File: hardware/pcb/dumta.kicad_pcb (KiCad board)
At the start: 2 copper layers, 111.3 x 90 mm, 48 parts, among them J2 nice_view, SW1 SW_PUSH, SW10 SW_PUSH, SW11 SW_PUSH, SW12 SW_PUSH, SW13 SW_PUSH, SW14 SW_PUSH, SW15 SW_PUSH, SW16 SW_PUSH, SW17 SW_PUSH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

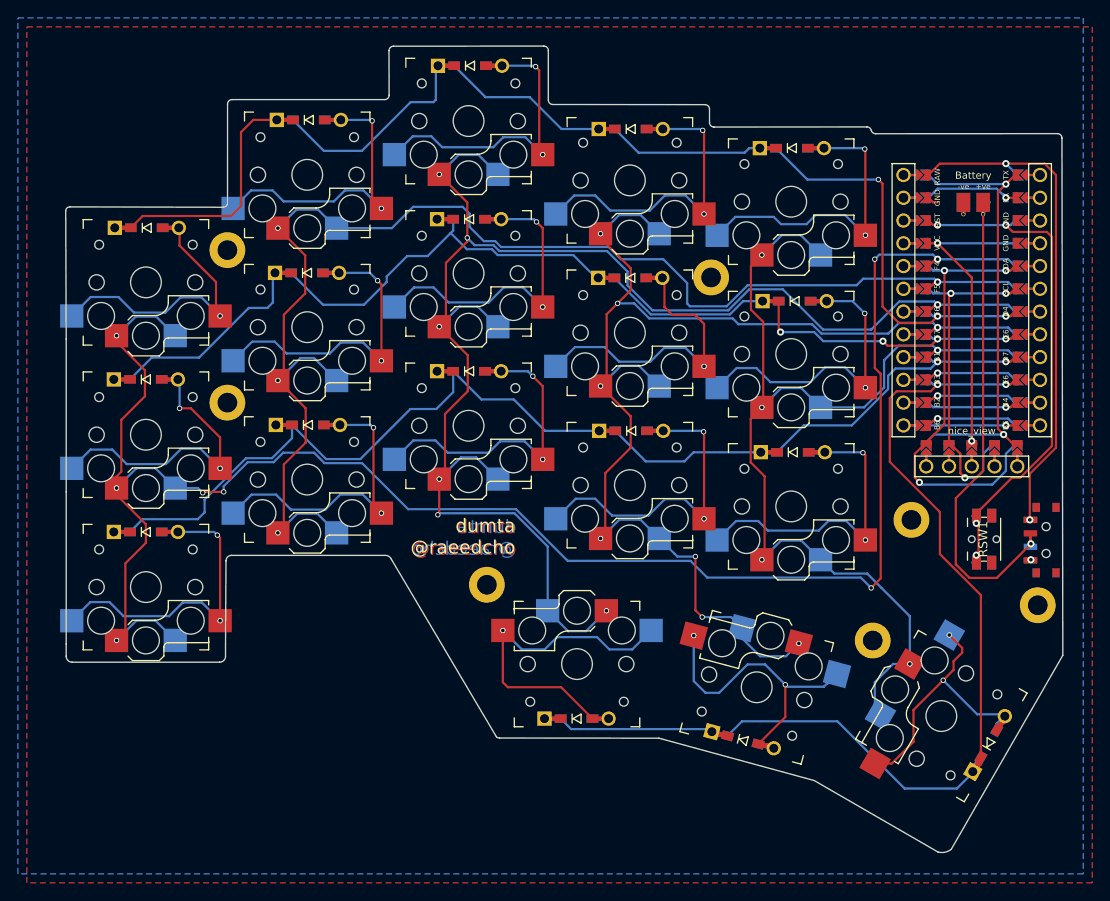
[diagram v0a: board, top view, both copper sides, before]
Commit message: feat: change footprints and alter them to match design rules
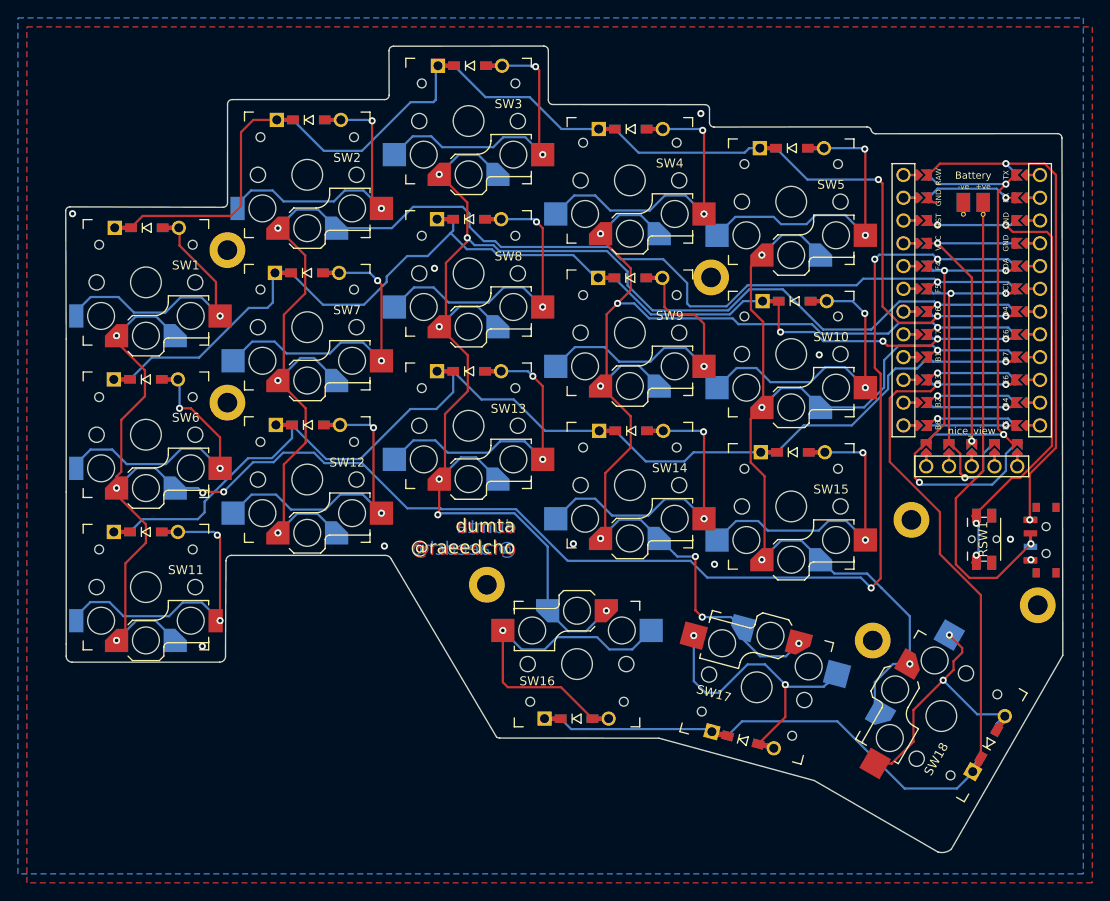
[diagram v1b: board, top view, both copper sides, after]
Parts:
- BT1: footprint swoop:Battery_pads_reversible -> dumta:Battery_pads_reversible
- D1, D10, D11, D12, D13, D14, D15, D16, D17, D18, D2, D3, D4, D5, D6, D7, D8, D9: footprint swoop:D_SMD_TH -> dumta:D_SMD_TH
- SW1, SW10, SW11, SW12, SW13, SW14, SW15, SW16, SW17, SW18, SW2, SW3, SW4, SW5, SW6, SW7, SW8, SW9: footprint keyswitches:Kailh_socket_PG1350_reversible -> dumta:Kailh_socket_PG1350_reversible
- U1: footprint swoop:ProMicro_jumpers -> dumta:ProMicro_jumpers
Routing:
- net col4: track 118.3 -> 116.2 mm
- net row2: track 139.8 -> 138.8 mm, vias 2 -> 1
- net Net-(BT1-+): track 55.3 -> 54.6 mm
- net GND: vias 0 -> 9

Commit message: fix: fix all major design rule errors
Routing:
- net GND: track 1.23 -> 27.6 mm, vias 9 -> 18
- net Net-(BT1-+): track 54.6 -> 50.9 mm
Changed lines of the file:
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@@
   (segment (start 163.068 119.38) (end 170.561 126.873) (width 0.25) (layer "B.Cu") (net 4))
   (segment (start 178.053166 125.222834) (end 178.053166 125.194992) (width 0.25) (layer "B.Cu") (net 4))
+  (segment (start 186.436 62.23) (end 186.944 61.722) (width 0.25) (layer "F.Cu") (net 5))
+  (segment (start 186.944 59.944) (end 186.69 59.69) (width 0.25) (layer "F.Cu") (net 5))
   (segment (start 173.736 61.468) (end 174.244 61.468) (width 0.25) (layer "F.Cu") (net 5))
+  (segment (start 182.753 63.5) (end 184.023 62.23) (width 0.25) (layer "F.Cu") (net 5))
   (segment (start 173.228 60.96) (end 173.736 61.468) (width 0.25) (layer "F.Cu") (net 5))
+  (segment (start 179.324 89.402) (end 179.324 91.948) (width 0.25) (layer "F.Cu") (net 5))
+  (segment (start 186.944 61.722) (end 186.944 59.944) (width 0.25) (layer "F.Cu") (net 5))
+  (segment (start 182.753 66.04) (end 182.626 66.04) (width 0.25) (layer "F.Cu") (net 5))
+  (segment (start 180.594 88.132) (end 179.324 89.402) (width 0.25) (layer "F.Cu") (net 5))
+  (segment (start 184.023 62.23) (end 186.436 62.23) (width 0.25) (layer "F.Cu") (net 5))
+  (segment (start 182.626 66.04) (end 181.864 65.278) (width 0.25) (layer "F.Cu") (net 5))
+  (via (at 186.69 59.69) (size 0.8) (drill 0.4) (layers "F.Cu" "B.Cu") (net 5))
   (via (at 133.604 99.568) (size 0.8) (drill 0.4) (layers "F.Cu" "B.Cu") (free) (net 5))
   (via (at 161.036 78.486) (size 0.8) (drill 0.4) (layers "F.Cu" "B.Cu") (free) (net 5))
+  (via (at 175.006 65.024) (size 0.8) (drill 0.4) (layers "F.Cu" "B.Cu") (net 5))
+  (via (at 166.116 71.882) (size 0.8) (drill 0.4) (layers "F.Cu" "B.Cu") (free) (net 5))
   (via (at 92.202 110.998) (size 0.8) (drill 0.4) (layers "F.Cu" "B.Cu") (free) (net 5))
-  (via (at 182.372 99.06) (size 0.8) (drill 0.4) (layers "F.Cu" "B.Cu") (free) (net 5))
   (via (at 149.352 101.854) (size 0.8) (drill 0.4) (layers "F.Cu" "B.Cu") (free) (net 5))
   (via (at 112.522 99.822) (size 0.8) (drill 0.4) (layers "F.Cu" "B.Cu") (free) (net 5))
+  (via (at 174.244 92.202) (size 0.8) (drill 0.4) (layers "F.Cu" "B.Cu") (net 5))
+  (via (at 175.514 58.42) (size 0.8) (drill 0.4) (layers "F.Cu" "B.Cu") (free) (net 5))
+  (via (at 106.934 92.456) (size 0.8) (drill 0.4) (layers "F.Cu" "B.Cu") (free) (net 5))
+  (via (at 165.1 78.486) (size 0.8) (drill 0.4) (layers "F.Cu" "B.Cu") (free) (net 5))
   (via (at 77.724 62.738) (size 0.8) (drill 0.4) (layers "F.Cu" "B.Cu") (free) (net 5))
   (via (at 118.11 68.834) (size 0.8) (drill 0.4) (layers "F.Cu" "B.Cu") (free) (net 5))
   (via (at 147.828 51.562) (size 0.8) (drill 0.4) (layers "F.Cu" "B.Cu") (free) (net 5))
-  (segment (start 178.054 69.85) (end 174.244 66.04) (width 0.25) (layer "F.Cu") (net 6))
+  (via (at 131.572 65.024) (size 0.8) (drill 0.4) (layers "F.Cu" "B.Cu") (free) (net 5))
+  (via (at 181.864 65.278) (size 0.8) (drill 0.4) (layers "F.Cu" "B.Cu") (free) (net 5))
+  (via (at 125.222 86.106) (size 0.8) (drill 0.4) (layers "F.Cu" "B.Cu") (free) (net 5))
+  (segment (start 176.616 60.96) (end 175.514 60.96) (width 0.25) (layer "B.Cu") (net 5))
+  (segment (start 174.244 89.402) (end 174.244 92.202) (width 0.25) (layer "B.Cu") (net 5))
+  (segment (start 184.023 59.69) (end 186.69 59.69) (width 0.25) (layer "B.Cu") (net 5))
+  (segment (start 173.355 63.5) (end 174.117 62.738) (width 0.25) (layer "B.Cu") (net 5))
+  (segment (start 173.355 66.04) (end 173.355 65.903695) (width 0.25) (layer "B.Cu") (net 5))
+  (segment (start 173.355 65.903695) (end 174.234695 65.024) (width 0.25) (layer "B.Cu") (net 5))
+  (segment (start 182.753 60.96) (end 184.023 59.69) (width 0.25) (layer "B.Cu") (net 5))
+  (segment (start 174.117 62.738) (end 174.498 62.738) (width 0.25) (layer "B.Cu") (net 5))
+  (segment (start 175.514 88.132) (end 174.244 89.402) (width 0.25) (layer "B.Cu") (net 5))
+  (segment (start 174.234695 65.024) (end 175.006 65.024) (width 0.25) (layer "B.Cu") (net 5))
+  (segment (start 176.53 86.5765) (end 176.53 68.326) (width 0.25) (layer "F.Cu") (net 6))
   (segment (start 173.228 66.04) (end 174.244 66.04) (width 0.25) (layer "F.Cu") (net 6))
-  (segment (start 178.054 88.1005) (end 178.054 69.85) (width 0.25) (layer "F.Cu") (net 6))
+  (segment (start 176.53 68.326) (end 174.244 66.04) (width 0.25) (layer "F.Cu") (net 6))
+  (segment (start 178.054 88.1005) (end 176.53 86.5765) (width 0.25) (layer "F.Cu") (net 6))
   (via (at 174.244 66.04) (size 0.8) (drill 0.4) (layers "F.Cu" "B.Cu") (net 6))
   (via (at 178.054 88.1005) (size 0.8) (drill 0.4) (layers "F.Cu" "B.Cu") (net 6))
@@
   (segment (start 171.144649 107.654649) (end 171.144649 112.978767) (width 0.25) (layer "B.Cu") (net 11))
   (segment (start 158.9606 65.1256) (end 156.8594 65.1256) (width 0.25) (layer "B.Cu") (net 11))
-  (segment (start 176.276 94.488) (end 179.324 91.44) (width 0.25) (layer "F.Cu") (net 12))
   (segment (start 184.602 98.404) (end 184.602 99.624) (width 0.25) (layer "F.Cu") (net 12))
   (segment (start 184.602 98.404) (end 184.602 99.512) (width 0.25) (layer "F.Cu") (net 12))
-  (segment (start 180.848 103.378) (end 177.8 103.378) (width 0.25) (layer "F.Cu") (net 12))
-  (segment (start 177.8 103.378) (end 176.276 101.854) (width 0.25) (layer "F.Cu") (net 12))
   (segment (start 184.602 99.512) (end 184.658 99.568) (width 0.25) (layer "F.Cu") (net 12))
-  (segment (start 184.602 99.624) (end 180.848 103.378) (width 0.25) (layer "F.Cu") (net 12))
-  (segment (start 176.276 101.854) (end 176.276 94.488) (width 0.25) (layer "F.Cu") (net 12))
-  (segment (start 179.324 91.44) (end 179.324 61.468) (width 0.25) (layer "F.Cu") (net 12))
   (via (at 184.658 99.568) (size 0.8) (drill 0.4) (layers "F.Cu" "B.Cu") (net 12))
+  (segment (start 182.88 98.806) (end 183.978 99.904) (width 0.25) (layer "B.Cu") (net 12))
+  (segment (start 187.452 90.678) (end 182.88 95.25) (width 0.25) (layer "B.Cu") (net 12))
+  (segment (start 187.452 63.246) (end 187.452 90.678) (width 0.25) (layer "B.Cu") (net 12))
+  (segment (start 186.436 62.23) (end 187.452 63.246) (width 0.25) (layer "B.Cu") (net 12))
+  (segment (start 182.88 95.25) (end 182.88 98.806) (width 0.25) (layer "B.Cu") (net 12))
+  (segment (start 180.086 62.23) (end 186.436 62.23) (width 0.25) (layer "B.Cu") (net 12))
+  (segment (start 183.978 99.904) (end 184.602 99.904) (width 0.25) (layer "B.Cu") (net 12))
+  (segment (start 179.324 61.468) (end 180.086 62.23) (width 0.25) (layer "B.Cu") (net 12))
   (segment (start 89.662 66.294) (end 89.662 64.4652) (width 0.25) (layer "F.Cu") (net 13))
   (segment (start 93.726 70.358) (end 89.662 66.294) (width 0.25) (layer "F.Cu") (net 13))
